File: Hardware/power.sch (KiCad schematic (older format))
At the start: 21 parts, among them IC201 FT232RQ, P201 USB_OTG, P202 CONN_01X02, U201 MCP1700T-3302E/TT

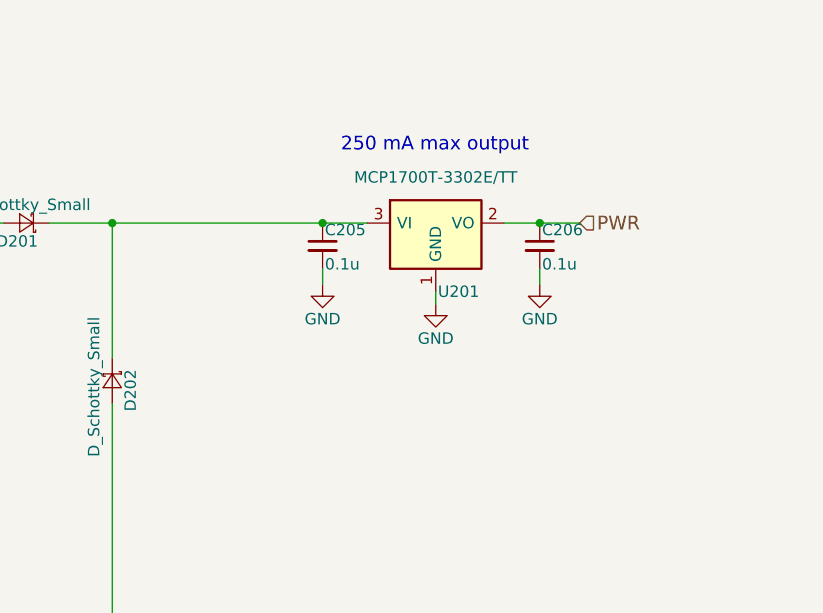
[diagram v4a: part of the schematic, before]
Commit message: fixed jst sh headers and added button footprint
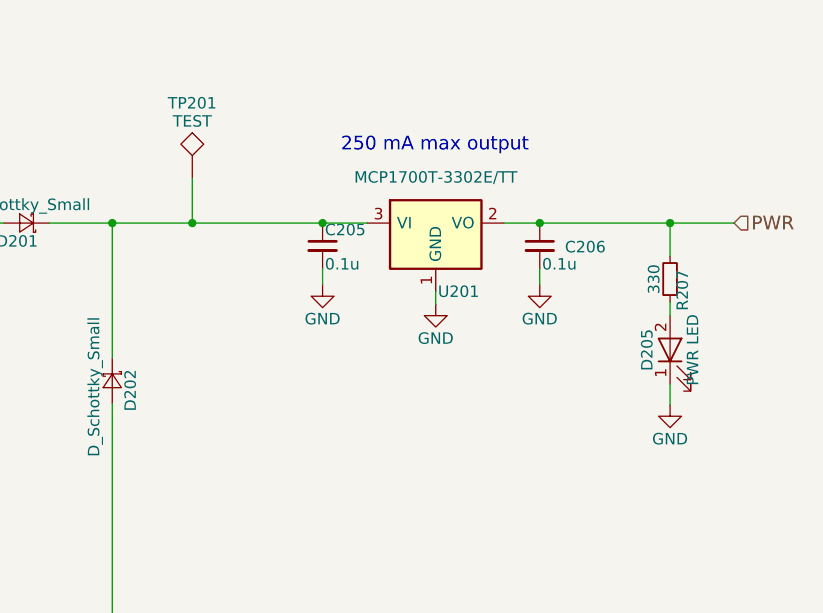
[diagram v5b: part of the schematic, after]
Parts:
- added D205: PWR LED, LEDs:LED_0805, symbol LED
- added R207: 330, Resistors_SMD:R_0805, symbol R_Small
- added TP201: TEST, Measurement_Points:Measurement_Point_Round-SMD-Pad_Small, symbol TEST
- C202: footprint Capacitors_SMD:C_1206 -> Capacitors_SMD:C_0805
- D201, D202: MPN (none) -> SK310A-TP; NOTE (none) -> locally sourced
- D203, D204: MPN (none) -> LTST-C171GKT; NOTE (none) -> locally sourced
- P201: Fieldname Value -> (none); NOTE (none) -> locally sourced
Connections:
- net GND: now also D205.1 (K)
- net PWR: now also R207.2
- net at C205.1, D201.1 (K), D202.1 (K)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: now also TP201.1
- new net: D205.2 (A), R207.1
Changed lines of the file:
@@
 F 0 "C202" H 4960 3745 50  0000 L CNN
 F 1 "4.7u" H 4960 3595 50  0000 L CNN
-F 2 "Capacitors_SMD:C_1206" H 4950 3675 50  0001 C CNN
+F 2 "Capacitors_SMD:C_0805" H 4950 3675 50  0001 C CNN
 F 3 "" H 4950 3675 50  0000 C CNN
 F 4 "Value" H 4950 3675 60  0001 C CNN "Fieldname"
@@
 U 1 1 58D7F457
 P 7310 1580
-F 0 "C206" H 7320 1650 50  0000 L CNN
+F 0 "C206" H 7420 1575 50  0000 L CNN
 F 1 "0.1u" H 7320 1500 50  0000 L CNN
 F 2 "Capacitors_SMD:C_0805" H 7310 1580 50  0001 C CNN
@@
 	1    0    0    -1
 $EndComp
-Text HLabel 7485 1480 2    60   Input ~ 0
+Text HLabel 8160 1480 2    60   Input ~ 0
 PWR
 $Comp
@@
 F 2 "CentralCommand:10118193" V 3415 4220 50  0001 C CNN
 F 3 "http://portal.fciconnect.com/Comergent//fci/drawing/10118193.pdf" V 3415 4220 50  0001 C CNN
-F 4 "Value" H 3465 4320 60  0001 C CNN "Fieldname"
+F 4 "locally sourced" H 3465 4320 60  0001 C CNN "NOTE"
 F 5 "10118193-0001LF" H 3465 4320 60  0001 C CNN "MPN"
 	1    3465 4320
@@
 F 2 "Diodes_SMD:D_0805" V 5065 1480 50  0001 C CNN
 F 3 "" V 5065 1480 50  0000 C CNN
+F 4 "locally sourced" H 5065 1480 60  0001 C CNN "NOTE"
+F 5 "SK310A-TP" H 5065 1480 60  0001 C CNN "MPN"
 	1    5065 1480
 	-1   0    0    1
@@
 F 2 "Diodes_SMD:D_0805" V 5440 2170 50  0001 C CNN
 F 3 "" V 5440 2170 50  0000 C CNN
+F 4 "locally sourced" H 5440 2170 60  0001 C CNN "NOTE"
+F 5 "SK310A-TP" H 5440 2170 60  0001 C CNN "MPN"
 	1    5440 2170
 	0    1    1    0
@@
 	1    0    0    -1
 $EndComp
-Wire Wire Line
-	4735 3525 5590 3525
-Wire Wire Line
-	5490 3525 5490 3625
-Wire Wire Line
-	4950 3525 4950 3575
-Wire Wire Line
-	5165 3525 5165 3575
-Connection ~ 5165 3525
-Wire Wire Line
-	5165 3830 5165 3775
-Wire Wire Line
-	4950 3830 5165 3830
-Wire Wire Line
-	5075 3830 5075 3870
-Wire Wire Line
-	4950 3830 4950 3775
-Connection ~ 5075 3830
-Wire Wire Line
-	5490 3625 5590 3625
-Connection ~ 5490 3525
-Wire Wire Line
-	5165 1480 6555 1480
-Wire Wire Line
-	6360 1680 6360 1750
-Wire Wire Line
-	7310 1680 7310 1750
-Wire Wire Line
-	7155 1480 7485 1480
-Wire Wire Line
-	6855 1780 6855 1835
-Connection ~ 7310 1480
-Connection ~ 4950 3525
-Wire Wire Line
-	4105 3525 4535 3525
-Wire Wire Line
-	4345 3725 4345 3790
-Connection ~ 4345 3525
-Wire Wire Line
-	3765 4120 4105 4120
-Wire Wire Line
-	4105 4120 4105 3525
-Wire Wire Line
-	3765 4220 5410 4220
-Wire Wire Line
-	5410 4220 5410 3765
-Wire Wire Line
-	5410 3765 5590 3765
-Wire Wire Line
-	3765 4320 5465 4320
-Wire Wire Line
-	5465 4320 5465 3885
-Wire Wire Line
-	5465 3885 5590 3885
-Wire Wire Line
-	3765 4520 3765 4850
-Wire Wire Line
-	3365 4720 3365 4800
-Wire Wire Line
-	3365 4800 3765 4800
-Connection ~ 3765 4800
-Wire Wire Line
-	5590 4685 5105 4685
-Connection ~ 6360 1480
-Wire Wire Line
-	4840 1580 4840 1720
-Wire Wire Line
-	4840 1480 4965 1480
-Wire Wire Line
-	5440 1480 5440 2070
-Connection ~ 5440 1480
-Wire Wire Line
-	5440 2270 5440 3335
-Wire Wire Line
-	5440 3335 4810 3335
-Wire Wire Line
-	4810 3335 4810 3525
-Connection ~ 4810 3525
-Wire Wire Line
-	5275 5095 5590 5095
-Wire Wire Line
-	5275 5295 5275 5345
-Wire Wire Line
-	7090 3505 7195 3505
-Wire Wire Line
-	7090 3615 7195 3615
-Wire Wire Line
-	7195 3755 7100 3755
-Wire Wire Line
-	7090 3885 7195 3885
-Wire Wire Line
-	7395 3885 7615 3885
-Wire Wire Line
-	7395 3755 7495 3755
-Wire Wire Line
-	7495 3755 7495 3885
-Connection ~ 7495 3885
 $Comp
 L LED D203
@@
 F 3 "" H 7890 4260 50  0000 C CNN
 F 4 "Value" H 7890 4260 60  0001 C CNN "Fieldname"
+F 5 "locally sourced" H 7890 4260 60  0001 C CNN "NOTE"
+F 6 "LTST-C171GKT" H 7890 4260 60  0001 C CNN "MPN"
 	1    7890 4260
 	0    -1   -1   0
@@
 F 2 "LEDs:LED_0805" H 8200 4265 50  0001 C CNN
 F 3 "" H 8200 4265 50  0000 C CNN
+F 4 "locally sourced" H 8200 4265 60  0001 C CNN "NOTE"
+F 5 "LTST-C171GKT" H 8200 4265 60  0001 C CNN "MPN"
 	1    8200 4265
 	0    -1   -1   0
@@
 	-1   0    0    1
 $EndComp
-Wire Wire Line
-	7890 4055 7890 4110
-Wire Wire Line
-	8200 4055 8200 4115
-Wire Wire Line
-	5440 3220 8055 3220
-Wire Wire Line
-	8055 3220 8055 3760
-Wire Wire Line
-	7890 3760 8200 3760
-Wire Wire Line
-	7890 3760 7890 3855
-Connection ~ 5440 3220
-Wire Wire Line
-	8200 3760 8200 3855
-Connection ~ 8055 3760
-Wire Wire Line
-	7395 3505 7685 3505
 Text HLabel 7685 3505 2    60   Input ~ 0
 TX
-Wire Wire Line
-	7395 3615 7685 3615
 Text HLabel 7685 3615 2    60   Input ~ 0
 RX
-Wire Wire Line
-	7090 4565 7890 4565
-Wire Wire Line
-	7890 4565 7890 4410
-Wire Wire Line
-	7100 4715 8200 4715
-Wire Wire Line
-	8200 4715 8200 4415
 Text Label 7285 4565 0    60   ~ 0
 TXLED
@@
 	1    0    0    -1
 $EndComp
+NoConn ~ 5590 4895
+NoConn ~ 5580 4995
+$Comp
+L LED D205
+U 1 1 58EB8302
+P 7880 2035
+F 0 "D205" H 7880 2135 50  0000 C CNN
+F 1 "PWR LED" H 7880 1935 50  0000 C CNN
+F 2 "LEDs:LED_0805" H 7880 2035 50  0001 C CNN
+F 3 "" H 7880 2035 50  0000 C CNN
+F 4 "Value" H 7880 2035 60  0001 C CNN "Fieldname"
+F 5 "locally sourced" H 7880 2035 60  0001 C CNN "NOTE"
+F 6 "LTST-C171GKT" H 7880 2035 60  0001 C CNN "MPN"
+	1    7880 2035
+	0    -1   -1   0
+$EndComp
+$Comp
+L R_Small R207
+U 1 1 58EB8309
+P 7880 1725
+F 0 "R207" V 7825 1685 50  0000 L CNN
+F 1 "330" V 7950 1660 50  0000 L CNN
+F 2 "Resistors_SMD:R_0805" H 7880 1725 50  0001 C CNN
+F 3 "" H 7880 1725 50  0000 C CNN
+F 4 "Value" H 7880 1725 60  0001 C CNN "Fieldname"
+	1    7880 1725
+	-1   0    0    1
+$EndComp
+Wire Wire Line
+	4735 3525 5590 3525
+Wire Wire Line
+	5490 3525 5490 3625
+Wire Wire Line
+	4950 3525 4950 3575
+Wire Wire Line
+	5165 3525 5165 3575
+Connection ~ 5165 3525
+Wire Wire Line
+	5165 3830 5165 3775
+Wire Wire Line
+	4950 3830 5165 3830
+Wire Wire Line
+	5075 3830 5075 3870
+Wire Wire Line
+	4950 3830 4950 3775
+Connection ~ 5075 3830
+Wire Wire Line
+	5490 3625 5590 3625
+Connection ~ 5490 3525
+Wire Wire Line
+	5165 1480 6555 1480
+Wire Wire Line
+	6360 1680 6360 1750
+Wire Wire Line
+	7310 1680 7310 1750
+Wire Wire Line
+	7155 1480 8160 1480
+Wire Wire Line
+	6855 1780 6855 1835
+Connection ~ 7310 1480
+Connection ~ 4950 3525
+Wire Wire Line
+	4105 3525 4535 3525
+Wire Wire Line
+	4345 3725 4345 3790
+Connection ~ 4345 3525
+Wire Wire Line
+	3765 4120 4105 4120
+Wire Wire Line
+	4105 4120 4105 3525
+Wire Wire Line
+	3765 4220 5410 4220
+Wire Wire Line
+	5410 4220 5410 3765
+Wire Wire Line
+	5410 3765 5590 3765
+Wire Wire Line
+	3765 4320 5465 4320
+Wire Wire Line
+	5465 4320 5465 3885
+Wire Wire Line
+	5465 3885 5590 3885
+Wire Wire Line
+	3765 4520 3765 4850
+Wire Wire Line
+	3365 4720 3365 4800
+Wire Wire Line
+	3365 4800 3765 4800
+Connection ~ 3765 4800
+Wire Wire Line
+	5590 4685 5105 4685
+Connection ~ 6360 1480
+Wire Wire Line
+	4840 1580 4840 1720
+Wire Wire Line
+	4840 1480 4965 1480
+Wire Wire Line
+	5440 1480 5440 2070
+Connection ~ 5440 1480
+Wire Wire Line
+	5440 2270 5440 3335
+Wire Wire Line
+	5440 3335 4810 3335
+Wire Wire Line
+	4810 3335 4810 3525
+Connection ~ 4810 3525
+Wire Wire Line
+	5275 5095 5590 5095
+Wire Wire Line
+	5275 5295 5275 5345
+Wire Wire Line
+	7090 3505 7195 3505
+Wire Wire Line
+	7090 3615 7195 3615
+Wire Wire Line
+	7195 3755 7100 3755
+Wire Wire Line
+	7090 3885 7195 3885
+Wire Wire Line
+	7395 3885 7615 3885
+Wire Wire Line
+	7395 3755 7495 3755
+Wire Wire Line
+	7495 3755 7495 3885
+Connection ~ 7495 3885
+Wire Wire Line
+	7890 4055 7890 4110
+Wire Wire Line
+	8200 4055 8200 4115
+Wire Wire Line
+	5440 3220 8055 3220
+Wire Wire Line
+	8055 3220 8055 3760
+Wire Wire Line
+	7890 3760 8200 3760
+Wire Wire Line
+	7890 3760 7890 3855
+Connection ~ 5440 3220
+Wire Wire Line
+	8200 3760 8200 3855
+Connection ~ 8055 3760
+Wire Wire Line
+	7395 3505 7685 3505
+Wire Wire Line
+	7395 3615 7685 3615
+Wire Wire Line
+	7090 4565 7890 4565
+Wire Wire Line
+	7890 4565 7890 4410
+Wire Wire Line
+	7100 4715 8200 4715
+Wire Wire Line
+	8200 4715 8200 4415
 Wire Wire Line
 	6570 5415 6570 5595
@@
 	6300 5480 6450 5480
 Connection ~ 6450 5480
-NoConn ~ 5590 4895
-NoConn ~ 5580 4995
+Wire Wire Line
+	7880 1825 7880 1885
+Wire Wire Line
+	7880 1480 7880 1625
+Connection ~ 7880 1480
+$Comp
+L GND #PWR019
+U 1 1 58EB8C6D
+P 7880 2275
+F 0 "#PWR019" H 7880 2025 50  0001 C CNN
+F 1 "GND" H 7880 2125 50  0000 C CNN
+F 2 "" H 7880 2275 50  0000 C CNN
+F 3 "" H 7880 2275 50  0000 C CNN
+	1    7880 2275
+	1    0    0    -1
+$EndComp
+Wire Wire Line
+	7880 2185 7880 2275
+$Comp
+L TEST TP201
+U 1 1 58EB9C20
+P 5790 1285
+F 0 "TP201" H 5790 1585 50  0000 C BNN
+F 1 "TEST" H 5790 1535 50  0000 C CNN
+F 2 "Measurement_Points:Measurement_Point_Round-SMD-Pad_Small" H 5790 1285 50  0001 C CNN
+F 3 "" H 5790 1285 50  0000 C CNN
+	1    5790 1285
+	1    0    0    -1
+$EndComp
+Wire Wire Line
+	5790 1285 5790 1480
+Connection ~ 5790 1480
 $EndSCHEMATC

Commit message: started board layout
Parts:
- P202: value CONN_01X02 -> POWER; Fieldname (none) -> Value
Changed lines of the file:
@@
 P 4640 1530
 F 0 "P202" H 4640 1680 50  0000 C CNN
-F 1 "CONN_01X02" V 4740 1530 50  0000 C CNN
+F 1 "POWER" V 4740 1530 50  0000 C CNN
 F 2 "Pin_Headers:Pin_Header_Straight_1x02" H 4640 1530 50  0001 C CNN
 F 3 "" H 4640 1530 50  0000 C CNN
+F 4 "Value" H 4640 1530 60  0001 C CNN "Fieldname"
 	1    4640 1530
 	-1   0    0    1

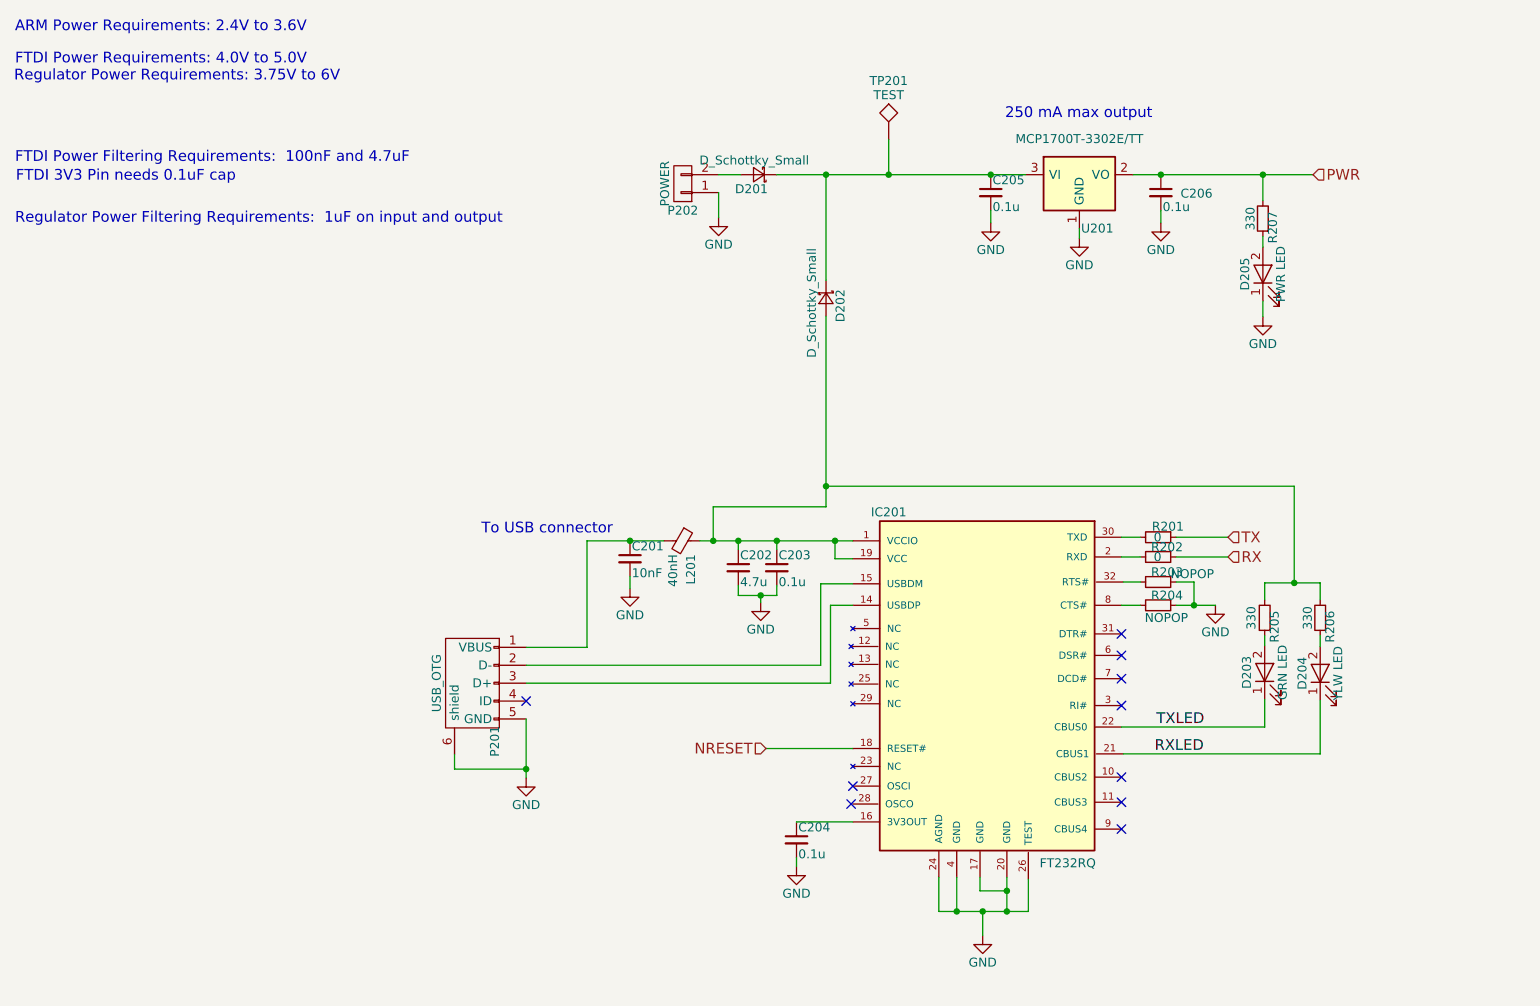
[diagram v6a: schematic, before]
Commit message: converted VCCIO to 3V3 and added 1x2 power and gnd
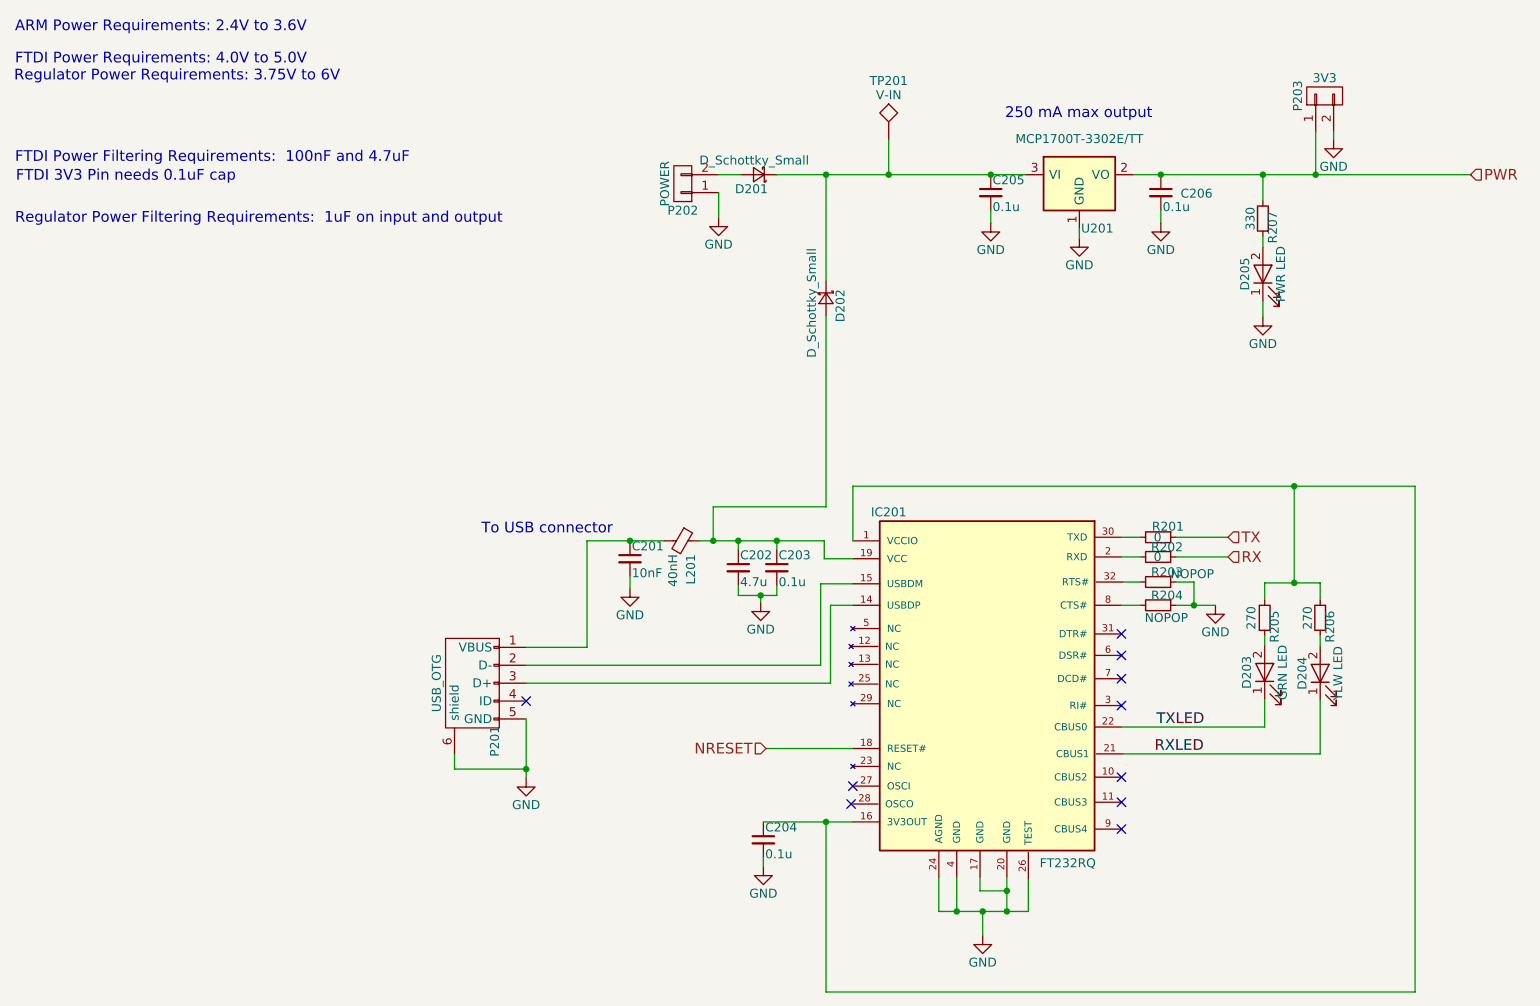
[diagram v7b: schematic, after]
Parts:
- added P203: 3V3, Pin_Headers:Pin_Header_Straight_1x02, symbol CONN_01X02
- R205, R206: value 330 -> 270
- TP201: value TEST -> V-IN
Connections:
- net GND: now also P203.2 (P2)
- net PWR: now also P203.1 (P1)
- net at C202.1, C203.1, D202.2 (A)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: no longer IC201.1 (VCCIO), R205.2, R206.2
- net at C204.1, IC201.16 (3V3OUT): now also IC201.1 (VCCIO), R205.2, R206.2
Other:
- moved on the sheet: C204
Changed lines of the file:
@@
 	1    0    0    -1
 $EndComp
-Text HLabel 8160 1480 2    60   Input ~ 0
+Text HLabel 9040 1480 2    60   Input ~ 0
 PWR
 $Comp
@@
 L C_Small C204
 U 1 1 58DEE911
-P 5275 5195
-F 0 "C204" H 5285 5265 50  0000 L CNN
-F 1 "0.1u" H 5285 5115 50  0000 L CNN
-F 2 "Capacitors_SMD:C_0805" H 5275 5195 50  0001 C CNN
-F 3 "" H 5275 5195 50  0000 C CNN
-F 4 "Value" H 5275 5195 60  0001 C CNN "Fieldname"
-	1    5275 5195
+P 5090 5195
+F 0 "C204" H 5100 5265 50  0000 L CNN
+F 1 "0.1u" H 5100 5115 50  0000 L CNN
+F 2 "Capacitors_SMD:C_0805" H 5090 5195 50  0001 C CNN
+F 3 "" H 5090 5195 50  0000 C CNN
+F 4 "Value" H 5090 5195 60  0001 C CNN "Fieldname"
+	1    5090 5195
 	1    0    0    -1
 $EndComp
@@
 L GND #PWR016
 U 1 1 58DEEABF
-P 5275 5345
-F 0 "#PWR016" H 5275 5095 50  0001 C CNN
-F 1 "GND" H 5275 5195 50  0000 C CNN
-F 2 "" H 5275 5345 50  0000 C CNN
-F 3 "" H 5275 5345 50  0000 C CNN
-	1    5275 5345
+P 5090 5345
+F 0 "#PWR016" H 5090 5095 50  0001 C CNN
+F 1 "GND" H 5090 5195 50  0000 C CNN
+F 2 "" H 5090 5345 50  0000 C CNN
+F 3 "" H 5090 5345 50  0000 C CNN
+	1    5090 5345
 	1    0    0    -1
 $EndComp
@@
 P 7890 3955
 F 0 "R205" V 7835 3915 50  0000 L CNN
-F 1 "330" V 7965 3890 50  0000 L CNN
+F 1 "270" V 7965 3890 50  0000 L CNN
 F 2 "Resistors_SMD:R_0805" H 7890 3955 50  0001 C CNN
 F 3 "" H 7890 3955 50  0000 C CNN
@@
 P 8200 3955
 F 0 "R206" V 8145 3915 50  0000 L CNN
-F 1 "330" V 8270 3890 50  0000 L CNN
+F 1 "270" V 8270 3890 50  0000 L CNN
 F 2 "Resistors_SMD:R_0805" H 8200 3955 50  0001 C CNN
 F 3 "" H 8200 3955 50  0000 C CNN
@@
 $EndComp
 Wire Wire Line
-	4735 3525 5590 3525
-Wire Wire Line
-	5490 3525 5490 3625
-Wire Wire Line
 	4950 3525 4950 3575
 Wire Wire Line
 	5165 3525 5165 3575
-Connection ~ 5165 3525
 Wire Wire Line
 	5165 3830 5165 3775
@@
 Connection ~ 5075 3830
 Wire Wire Line
-	5490 3625 5590 3625
-Connection ~ 5490 3525
-Wire Wire Line
 	5165 1480 6555 1480
 Wire Wire Line
@@
 	7310 1680 7310 1750
 Wire Wire Line
-	7155 1480 8160 1480
+	7155 1480 9040 1480
 Wire Wire Line
 	6855 1780 6855 1835
 Connection ~ 7310 1480
-Connection ~ 4950 3525
 Wire Wire Line
 	4105 3525 4535 3525
@@
 Wire Wire Line
 	4810 3335 4810 3525
-Connection ~ 4810 3525
-Wire Wire Line
-	5275 5095 5590 5095
-Wire Wire Line
-	5275 5295 5275 5345
+Wire Wire Line
+	5090 5295 5090 5345
 Wire Wire Line
 	7090 3505 7195 3505
@@
 	8200 4055 8200 4115
 Wire Wire Line
-	5440 3220 8055 3220
-Wire Wire Line
 	8055 3220 8055 3760
 Wire Wire Line
@@
 Wire Wire Line
 	7890 3760 7890 3855
-Connection ~ 5440 3220
 Wire Wire Line
 	8200 3760 8200 3855
@@
 	8200 4715 8200 4415
 Wire Wire Line
-	6570 5415 6570 5595
-Wire Wire Line
-	6570 5595 6070 5595
+	6570 5595 6570 5415
+Wire Wire Line
+	6070 5595 6570 5595
 Wire Wire Line
 	6070 5595 6070 5405
@@
 P 5790 1285
 F 0 "TP201" H 5790 1585 50  0000 C BNN
-F 1 "TEST" H 5790 1535 50  0000 C CNN
+F 1 "V-IN" H 5790 1535 50  0000 C CNN
 F 2 "Measurement_Points:Measurement_Point_Round-SMD-Pad_Small" H 5790 1285 50  0001 C CNN
 F 3 "" H 5790 1285 50  0000 C CNN
@@
 	5790 1285 5790 1480
 Connection ~ 5790 1480
+Wire Wire Line
+	5090 5095 5590 5095
+Wire Wire Line
+	5440 5095 5440 6045
+Wire Wire Line
+	5440 6045 8730 6045
+Wire Wire Line
+	8730 6045 8730 3220
+Wire Wire Line
+	8730 3220 5590 3220
+Connection ~ 5440 5095
+Wire Wire Line
+	5590 3220 5590 3525
+Connection ~ 8055 3220
+Wire Wire Line
+	5590 3625 5430 3625
+Wire Wire Line
+	5430 3625 5430 3525
+Wire Wire Line
+	5430 3525 4735 3525
+Connection ~ 5165 3525
+Connection ~ 4950 3525
+Connection ~ 4810 3525
+$Comp
+L CONN_01X02 P203
+U 1 1 591371DE
+P 8225 1040
+F 0 "P203" H 8225 1190 50  0000 C CNN
+F 1 "3V3" V 8325 1040 50  0000 C CNN
+F 2 "Pin_Headers:Pin_Header_Straight_1x02" H 8225 1040 50  0001 C CNN
+F 3 "" H 8225 1040 50  0000 C CNN
+F 4 "Value" H 8225 1040 60  0001 C CNN "Fieldname"
+	1    8225 1040
+	0    -1   -1   0
+$EndComp
+Wire Wire Line
+	8175 1240 8175 1480
+Connection ~ 8175 1480
+$Comp
+L GND #PWR020
+U 1 1 59137A62
+P 8275 1285
+F 0 "#PWR020" H 8275 1035 50  0001 C CNN
+F 1 "GND" H 8275 1135 50  0000 C CNN
+F 2 "" H 8275 1285 50  0000 C CNN
+F 3 "" H 8275 1285 50  0000 C CNN
+	1    8275 1285
+	1    0    0    -1
+$EndComp
+Wire Wire Line
+	8275 1240 8275 1285
 $EndSCHEMATC
